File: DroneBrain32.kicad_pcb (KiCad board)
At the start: 2 copper layers, 44 parts, among them J1 HEADER1X2, J10 HEADER1X10, J11 IMU_MH, J2 AIN0, J3 JTAG, J4 AIN1, J5 GPS, J6 USB-MINI-A, J7 IMU, J8 HEADER1X10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

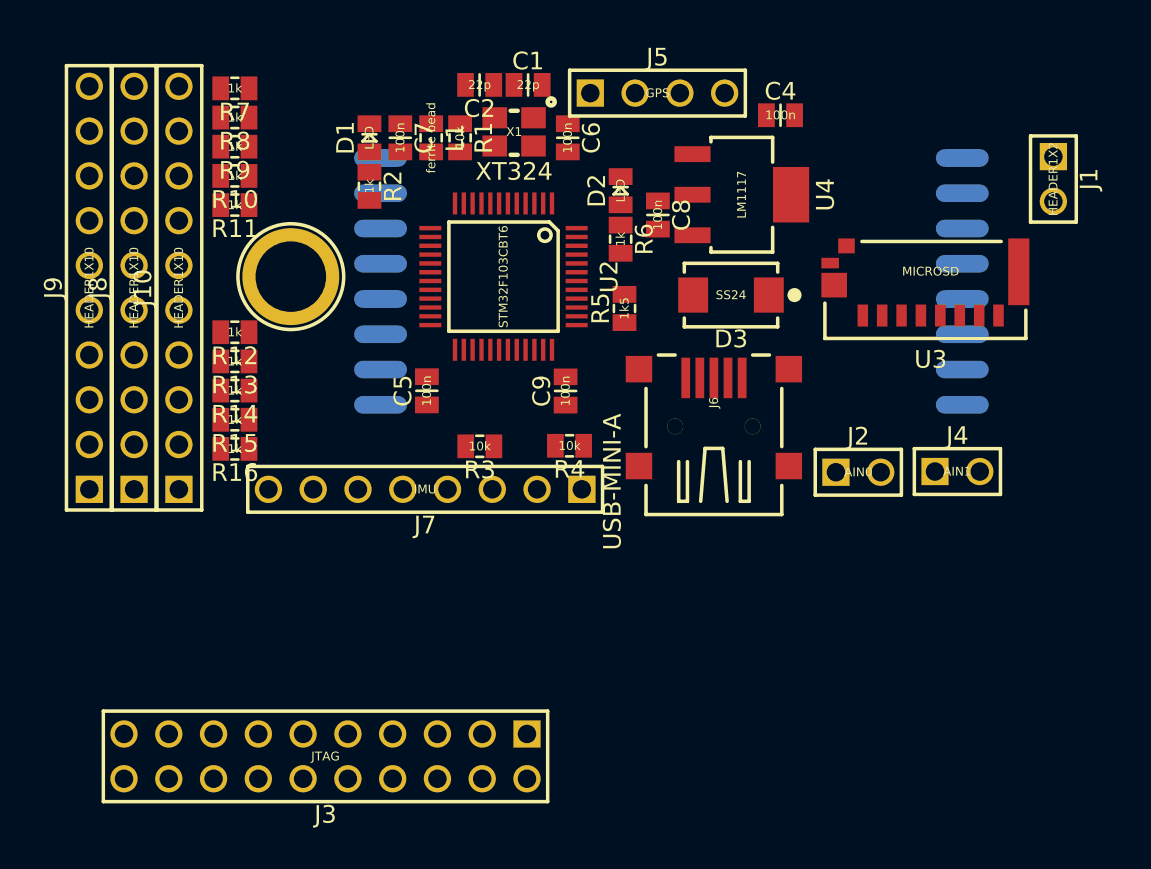
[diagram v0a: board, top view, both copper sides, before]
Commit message: Continuing component placement, started routing
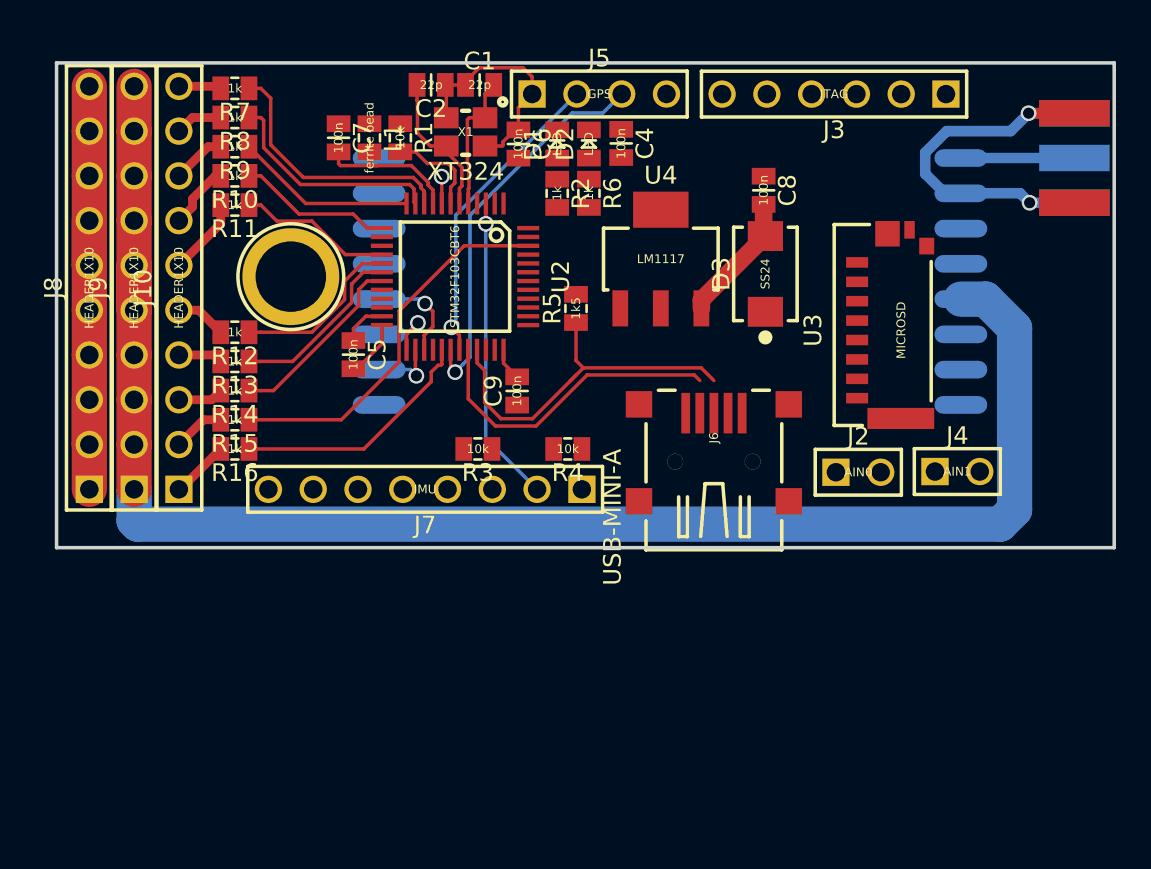
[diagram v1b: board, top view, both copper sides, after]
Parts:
- J1: footprint PinHead:HEADER1x2V -> Newlib:CON_SMA-Edge; moved to B.Cu
- J3: footprint PinHead:HEADER2x10V -> PinHead:HEADER1x6V
- moved J3 43.4 mm to (198.5, 100.8)
- moved R2 10.7 mm to (176.4, 106.4)
- moved D1 10.7 mm to (176.4, 103.6)
- moved C4 9.18 mm to (180.0, 103.6), turned to 270 degrees
- moved C8 6.16 mm to (188.1, 106.2)
- moved U4 5.87 mm to (182.3, 110.1), turned to 0 degrees
- moved C5 4.64 mm to (164.8, 115.5), turned to 270 degrees
- moved U3 4.26 mm to (193.4, 114.2), turned to 90 degrees
- moved J1 3.73 mm to (208.3, 104.4), turned to 180 degrees
- moved C7 3.50 mm to (164.0, 103.2)
- moved L1 3.50 mm to (165.8, 103.2)
- moved R1 3.39 mm to (167.5, 103.2)
- moved J5 3.30 mm to (175.0, 100.8)
- moved D2 3.20 mm to (178.2, 103.6)
- moved R6 3.16 mm to (178.2, 106.4)
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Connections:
- J3 pad 1: +3V3 -> GND
- J3 pad 2: +3V3 -> /NRST
- J3 pad 3: /NJTRST -> /TDO
- J3 pad 4: GND -> /TCK
- J3 pad 5: /TDI -> /TMS
- J3 pad 6: GND -> /TDI
- U1 pad 1: Net-(J1-Pad1) -> Net-(J1-Pad2)
- U1 pad 2: Net-(J1-Pad2) -> Net-(J1-Pad1)
- U2 pad 40: /NJTRST -> (no net)
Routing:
- net +5V: track 0.00 -> 99.2 mm
- net GND: track 0.00 -> 45.3 mm, vias 0 -> 1
- net Net-(J1-Pad1): track 0.00 -> 22.3 mm, vias 0 -> 2
- net /Tx: track 0.00 -> 22.1 mm, vias 0 -> 1
- net /RSSI: track 0.00 -> 21.6 mm
- net /USB_DP: track 0.00 -> 21.3 mm
- net /USB_DM: track 0.00 -> 17.9 mm
- net /Rx: track 0.00 -> 17.6 mm, vias 0 -> 1
- net /IMU_INTA: track 0.00 -> 17.4 mm, vias 0 -> 1
- net /CH1: track 0.00 -> 14.7 mm
- net /PPM: track 0.00 -> 14.1 mm
- net /CH2: track 0.00 -> 12.8 mm
- net /CH8: track 0.00 -> 10.6 mm
- net /CH3: track 0.00 -> 10.3 mm
- net /CH7: track 0.00 -> 10.2 mm
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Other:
- board outline added: 60 x 27.5 mm
- net class Default: clearance 0.254 -> 0.2; trace_width 0.254 -> 0.2
- rule trace_clearance: 0.254 -> 0.2
- rule trace_min: 0.254 -> 0.2

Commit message: Finished routing - first iteration
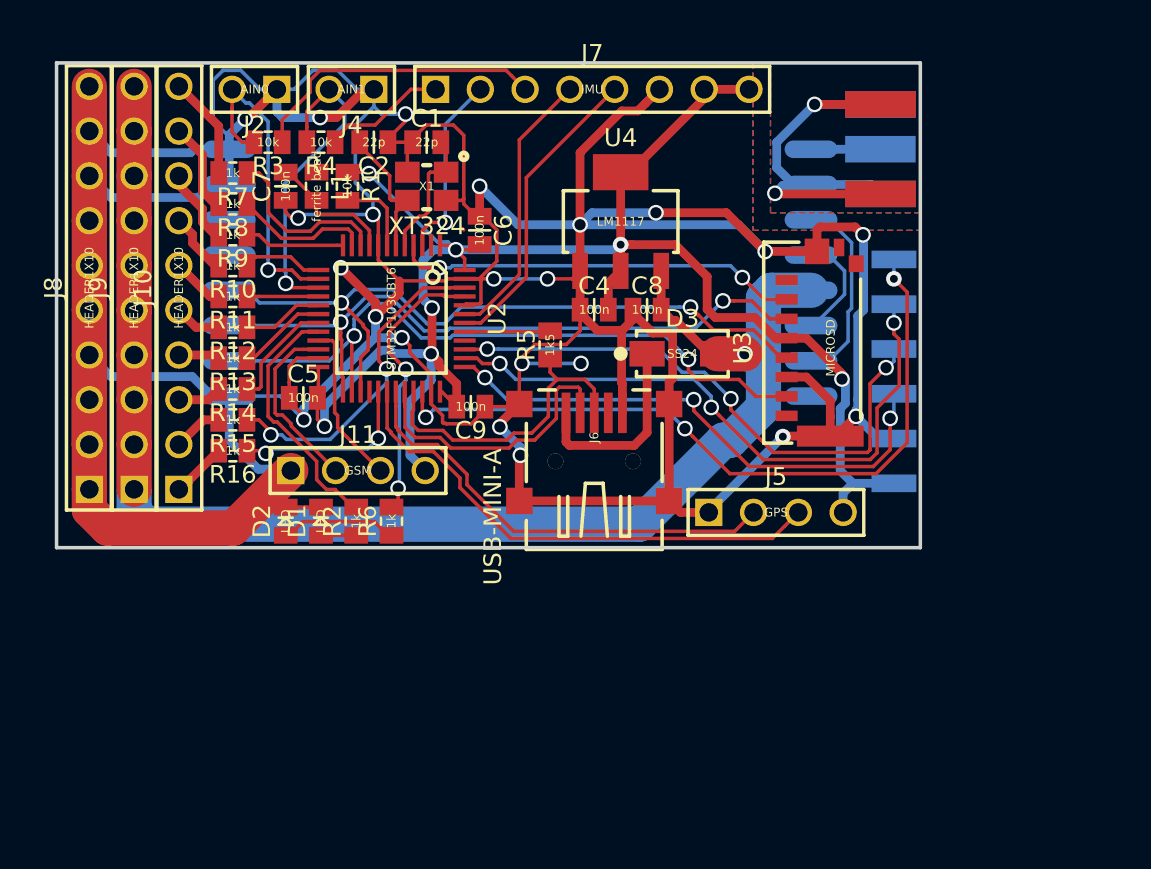
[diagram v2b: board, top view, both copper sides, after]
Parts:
- D3: footprint Newlib:SMB -> Newlib:SMA
- J11: value IMU_MH -> GSM; footprint Newlib:MountHole_D4P6 -> PinHead:HEADER1x4V
- J3: footprint PinHead:HEADER1x6V -> PinHead:HEADER1x6EF; moved to B.Cu
- moved J4 38.5 mm to (166.0, 100.5), turned to 180 degrees
- moved J2 38.4 mm to (160.5, 100.5), turned to 180 degrees
- moved D2 27.5 mm to (161.0, 125.0)
- moved J5 25.8 mm to (185.0, 124.5)
- moved D1 25.2 mm to (163.0, 125.0)
- moved J7 24.2 mm to (169.5, 100.5), turned to 0 degrees
- moved R4 22.3 mm to (163.0, 103.5)
- moved R2 21.8 mm to (165.0, 125.0), turned to 90 degrees
- moved R6 21.7 mm to (167.0, 125.0), turned to 90 degrees
- moved R3 21.1 mm to (160.0, 103.5)
- moved J3 16.0 mm to (195.5, 116.5), turned to 90 degrees
- moved J1 11.0 mm to (197.3, 103.9)
- moved J11 11.0 mm to (161.3, 122.1)
- moved C4 9.55 mm to (178.5, 113.0), turned to 0 degrees
- moved C8 9.47 mm to (181.5, 113.0), turned to 0 degrees
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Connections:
- J3 pad 1: GND -> +3V3
- J3 pad 2: /NRST -> GND
- J3 pad 3: /TDO -> /TCK
- J3 pad 4: /TCK -> /TDO
- J3 pad 5: /TMS -> /TDI
- J3 pad 6: /TDI -> /TMS
- J6 pad 4: (no net) -> Net-(J6-Pad4)
- L1 pad 1: (no net) -> Net-(L1-Pad1)
- U1 pad 13: (no net) -> /NSEL1
- U1 pad 14: (no net) -> /NIRQ1
- U1 pad 8: (no net) -> Net-(U1-Pad8)
- U2 pad 2: (no net) -> /NIRQ_RFM
- U2 pad 21: (no net) -> /SCL
- U2 pad 22: (no net) -> /SDA
- U2 pad 28: (no net) -> /NSEL_RFM
- U2 pad 40: (no net) -> /NJTRST
- U3 pad 1: (no net) -> Net-(U3-Pad1)
- U3 pad 10: (no net) -> Net-(U3-Pad10)
- U3 pad 8: (no net) -> Net-(U3-Pad8)
- U3 pad 9: (no net) -> Net-(U3-Pad9)
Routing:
- net GND: track 45.3 -> 327.7 mm, vias 1 -> 22
- net +3V3: track 5.11 -> 98.9 mm, vias 0 -> 7
- net /TMS: track 0.00 -> 42.0 mm, vias 0 -> 3
- net /MISO: track 3.69 -> 39.4 mm, vias 1 -> 2
- net /TDI: track 0.00 -> 35.4 mm, vias 0 -> 3
- net /SCK: track 5.64 -> 40.5 mm, vias 1 -> 2
- net /MOSI: track 4.18 -> 38.2 mm, vias 1 -> 2
- net /TDO: track 0.00 -> 32.2 mm, vias 0 -> 3
- net /TCK: track 0.00 -> 30.5 mm, vias 0 -> 3
- net /NSEL_SD: track 0.00 -> 23.0 mm, vias 0 -> 2
- net Net-(J4-Pad2): track 0.00 -> 18.3 mm, vias 0 -> 1
- net Net-(J2-Pad2): track 0.00 -> 18.2 mm, vias 0 -> 1
- net +5V: track 99.2 -> 81.0 mm, vias 0 -> 1
- net /IMU_SCL: track 0.00 -> 17.3 mm
- net /IMU_FSYNC: track 0.00 -> 17.0 mm
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- added copper zone on B.Cu, net GND
- added copper zone on F.Cu, net GND
- added copper zone on B.Cu, net Net-(J1-Pad1)
- added copper zone on F.Cu, net Net-(J1-Pad1)
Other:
- board size 60 x 27.5 mm -> 49 x 27.5 mm

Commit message: Finished board.
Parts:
- moved J7 18.0 mm to (187.5, 100.5), turned to 180 degrees
- moved C7 0.71 mm to (161.5, 106.5)
- moved L1 0.50 mm to (163.2, 106.0)
- moved R1 0.50 mm to (165.0, 106.0)
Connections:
- J1 pad 1: Net-(J1-Pad1) -> GND
- J7 pad 1: /IMU_DRDY -> +3V3
- J7 pad 2: /IMU_INTA -> +3V3
- J7 pad 3: /IMU_FSYNC -> GND
- J7 pad 4: /IMU_SDA -> /IMU_SCL
- J7 pad 5: /IMU_SCL -> /IMU_SDA
- J7 pad 6: GND -> /IMU_FSYNC
- J7 pad 7: +3V3 -> /IMU_INTA
- J7 pad 8: +3V3 -> /IMU_DRDY
- U1 pad 13: /NSEL1 -> /NSEL_RFM
- U1 pad 14: /NIRQ1 -> /NIRQ_RFM
- U1 pad 2: Net-(J1-Pad1) -> GND
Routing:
- net Net-(J1-Pad1): track 26.7 -> 0.00 mm, vias 2 -> 0
- net GND: track 327.7 -> 350.5 mm, vias 22 -> 27
- net /NIRQ_RFM: track 0.00 -> 15.6 mm, vias 0 -> 1
- net /NSEL_RFM: track 0.00 -> 14.2 mm, vias 0 -> 1
- net Net-(J4-Pad2): track 18.3 -> 13.7 mm, vias 1 -> 2
- net Net-(J2-Pad2): track 18.2 -> 14.1 mm, vias 1 -> 2
- net +3V3: track 98.9 -> 102.4 mm, vias 7 -> 8
- net /IMU_INTA: track 10.7 -> 14.0 mm, vias 1 -> 2
- net /MISO: track 39.4 -> 37.1 mm
- net /RSSI: track 18.8 -> 16.9 mm
- net /SCK: track 40.5 -> 38.9 mm
- net /MOSI: track 38.2 -> 36.9 mm
- net /NSEL_SD: track 23.0 -> 24.4 mm
- net +5V: track 81.0 -> 82.2 mm
- net /CH2: track 7.78 -> 8.81 mm
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- removed copper zone on B.Cu, net Net-(J1-Pad1)
- removed copper zone on F.Cu, net Net-(J1-Pad1)
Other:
- net class Default: via_dia 0.889 -> 0.5; via_drill 0.635 -> 0.35
- rule via_min_drill: 0.508 -> 0.35
- rule via_min_size: 0.889 -> 0.5
- board text added: "- + s"
- board text added: "GPS"
- board text added: "GSM"
- board text added: "IMU"

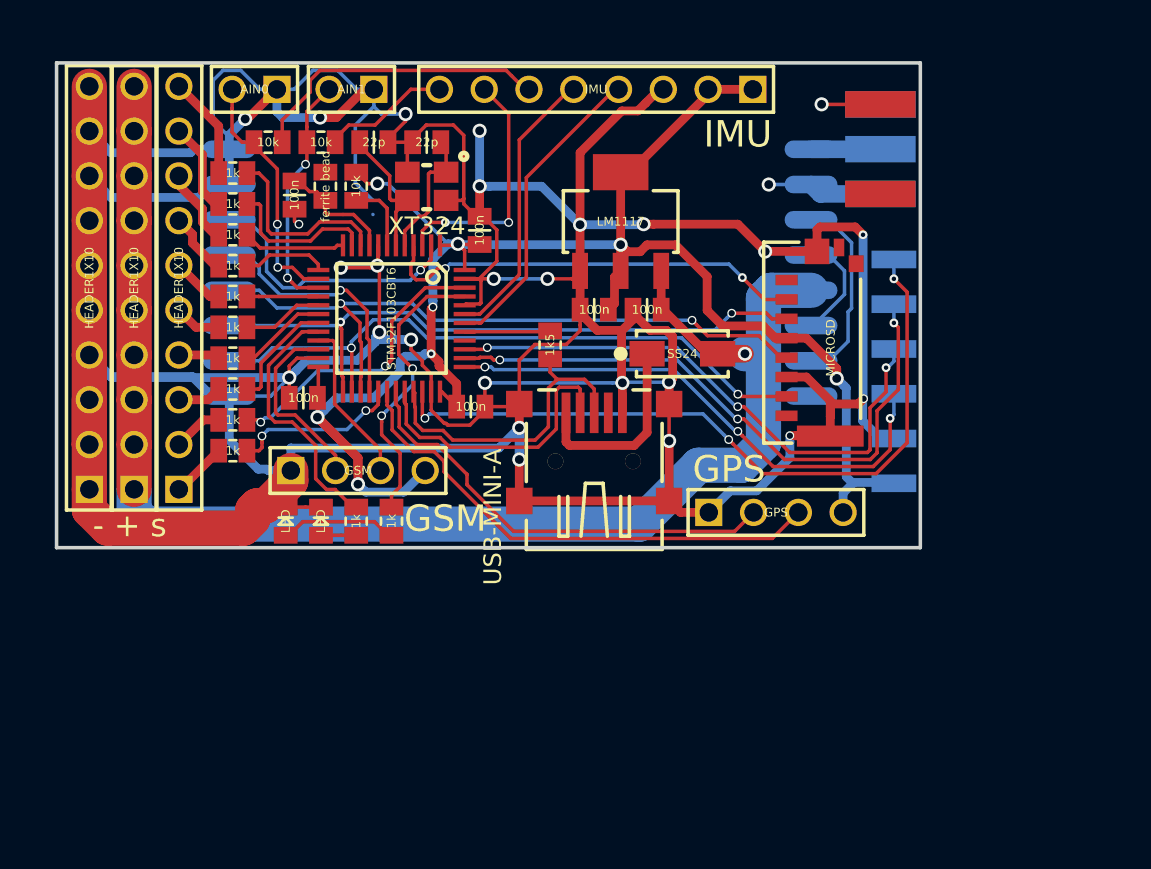
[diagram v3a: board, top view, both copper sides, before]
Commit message: Fixed vias for EC production
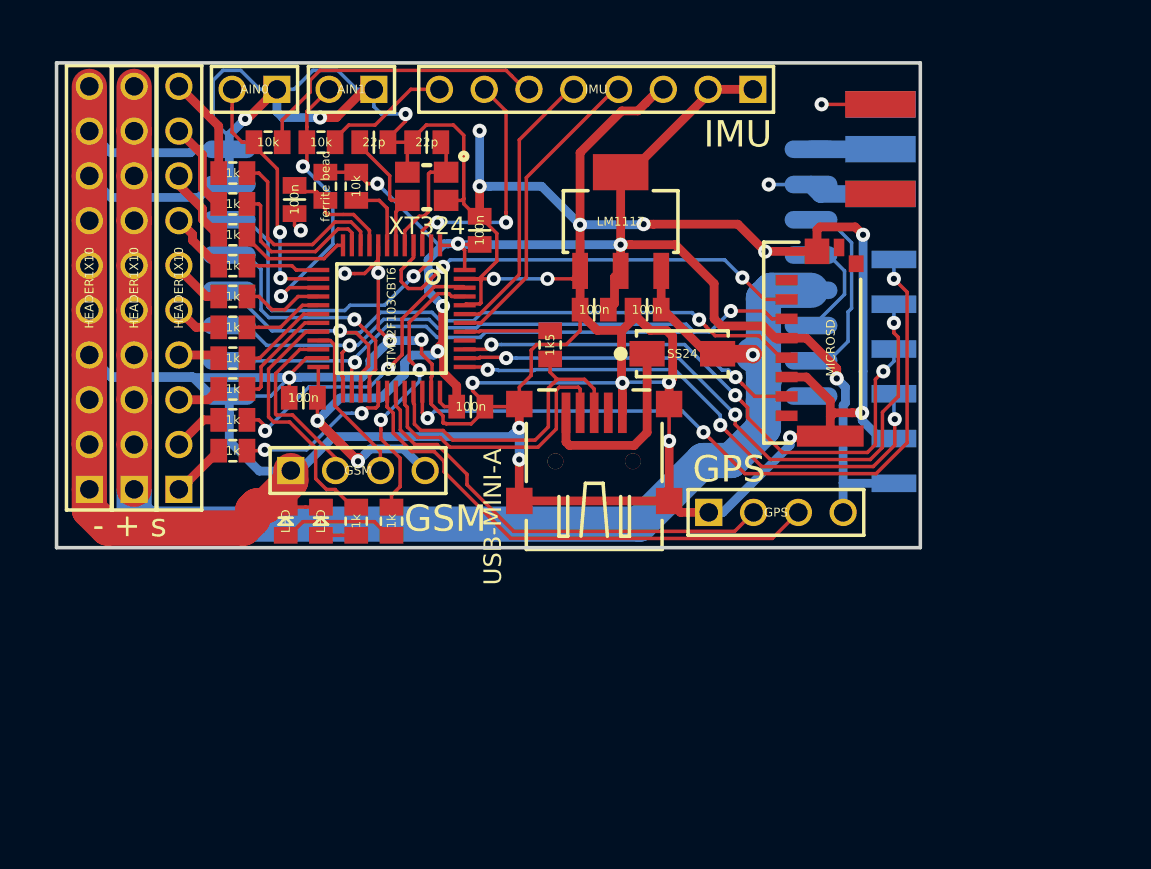
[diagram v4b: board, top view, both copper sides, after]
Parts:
- moved C7 0.25 mm to (161.5, 106.8)
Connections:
- L1 pad 1: Net-(L1-Pad1) -> +3V3
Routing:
- net GND: track 350.5 -> 344.0 mm
- net +3V3: track 102.4 -> 106.2 mm
- net Net-(J4-Pad2): track 13.7 -> 16.7 mm
- net /NIRQ_RFM: track 15.6 -> 17.8 mm
- net /NSEL_SD: track 24.4 -> 26.0 mm
- net /MISO: track 37.1 -> 36.3 mm
- net /CH2: track 8.81 -> 9.58 mm
- net /CH1: track 10.8 -> 11.5 mm
- net /CH4: track 4.84 -> 4.15 mm
- net /CH5: track 4.05 -> 4.67 mm
- net /CH3: track 5.82 -> 6.42 mm
- net /RSSI: track 16.9 -> 17.4 mm
- net /NSEL_RFM: track 14.2 -> 14.7 mm
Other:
- net class Default: via_dia 0.5 -> 0.8
- rule via_min_size: 0.5 -> 0.8

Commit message: Added decals
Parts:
- added G***: LOGO, Decals:jet, F.Cu at (186.6, 107.5)
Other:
- board text added: "DroneBrain32"
- board text added: "MZ 2014"

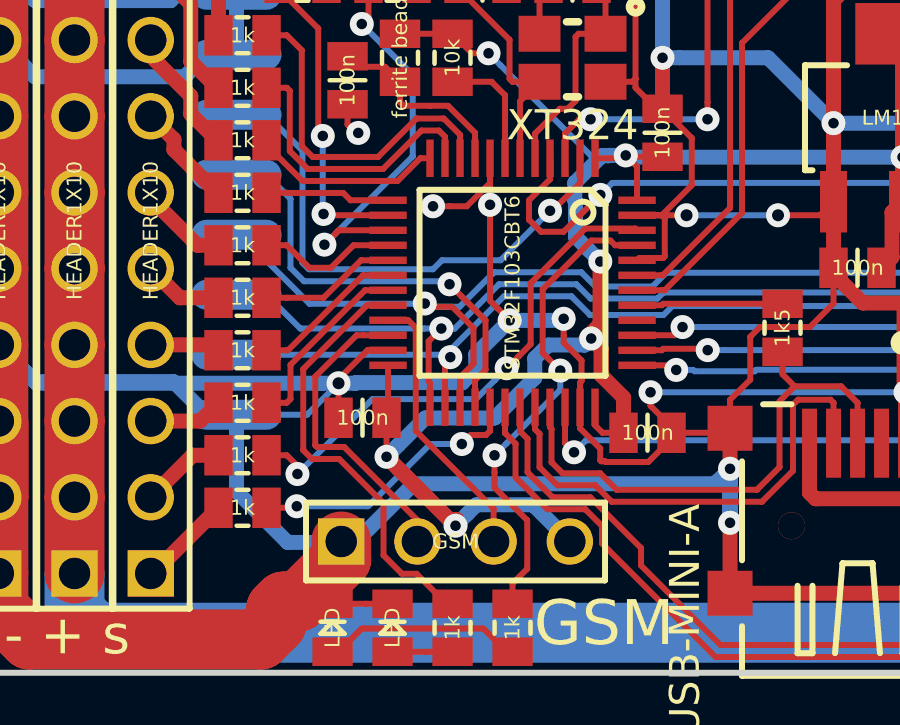
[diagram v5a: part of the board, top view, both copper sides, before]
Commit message: Fixed incorrect RFM23BP SPI pins assignment
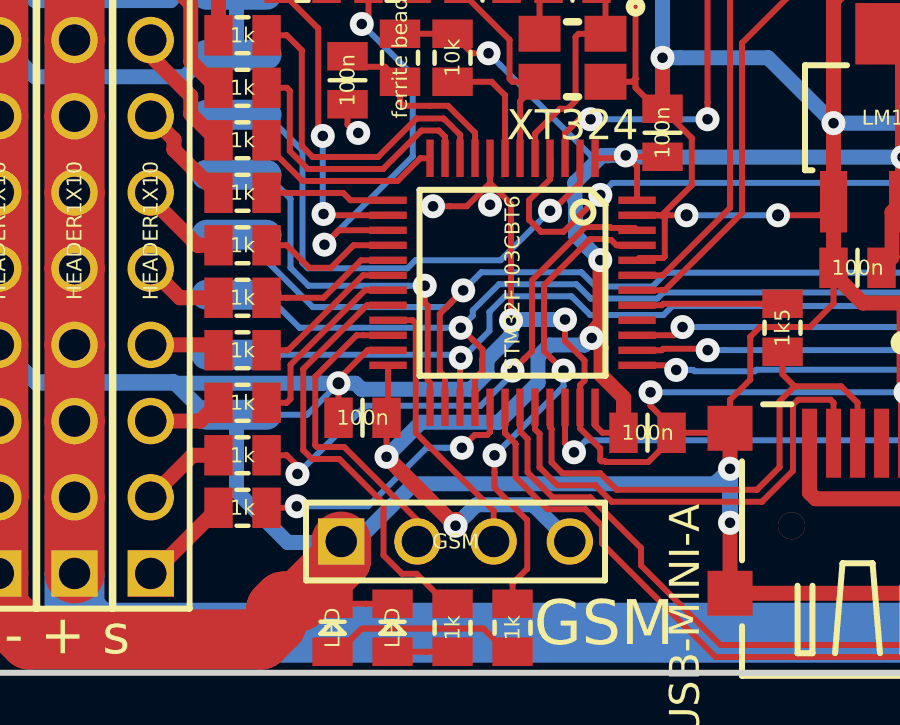
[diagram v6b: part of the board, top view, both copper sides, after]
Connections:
- U2 pad 25: /MOSI -> /NSEL_RFM
- U2 pad 26: /MISO -> /SCK
- U2 pad 27: /SCK -> /MISO
- U2 pad 28: /NSEL_RFM -> /MOSI
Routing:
- net /NSEL_RFM: track 14.7 -> 13.3 mm
- net GND: track 344.0 -> 344.6 mm
